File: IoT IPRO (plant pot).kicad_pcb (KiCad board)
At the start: 2 copper layers, 82 x 56 mm, 15 parts, among them Q1 Q_DUAL_NMOS_S1G1S2G2D1D1D2D2, U1 DS18S20, U3 AP9101C-SOT25

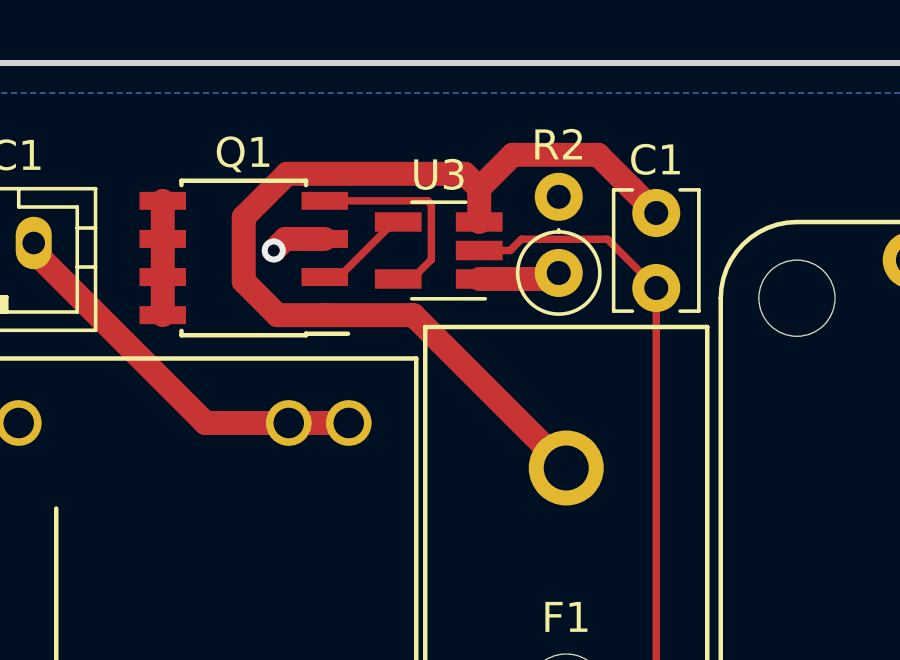
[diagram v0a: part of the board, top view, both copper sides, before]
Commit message: Switch AP9101C to SOT-26 :(
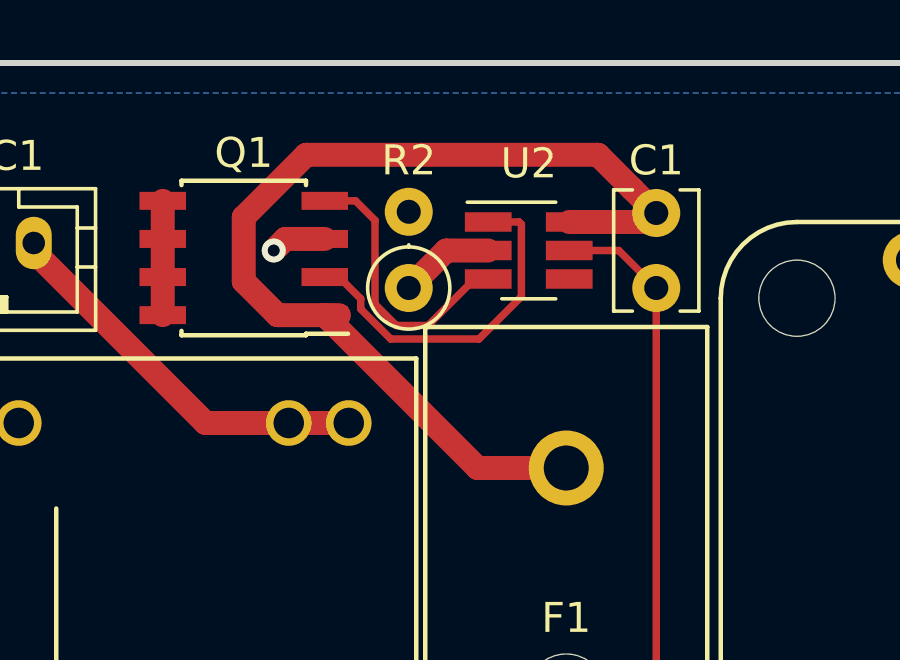
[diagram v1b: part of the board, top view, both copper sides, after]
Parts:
- removed U3: AP9101C-SOT25, Package_TO_SOT_SMD:SOT-23-5_HandSoldering
- added U2: AP9101C-SOT26, TO_SOT_Packages_SMD:SOT-23-6_Handsoldering, F.Cu at (81.5, 38.2)
- moved R2 5.02 mm to (77.5, 39.5)
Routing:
- net Net-(Q1-Pad2): track 3.21 -> 11.7 mm
- net Net-(C1-Pad1): track 30.4 -> 27.1 mm
- net Net-(Q1-Pad4): track 6.81 -> 9.45 mm
- net Net-(C1-Pad2): track 32.4 -> 34.4 mm

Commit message: Generate v1 Gerbers
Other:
- rule pad_to_mask_clearance: 0 -> 0.1
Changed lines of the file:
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@@
     (pad_size 1.5 1.5)
     (pad_drill 0.6)
-    (pad_to_mask_clearance 0)
+    (pad_to_mask_clearance 0.1)
     (solder_mask_min_width 0.25)
     (aux_axis_origin 0 0)
     (visible_elements 7FFFFFFF)
     (pcbplotparams
-      (layerselection 0x010fc_ffffffff)
+      (layerselection 0x010f0_ffffffff)
       (usegerberextensions false)
-      (usegerberattributes false)
+      (usegerberattributes true)
       (usegerberadvancedattributes false)
       (creategerberjobfile false)
@@
       (outputformat 1)
       (mirror false)
-      (drillshape 1)
+      (drillshape 0)
       (scaleselection 1)
-      (outputdirectory ""))
+      (outputdirectory "fab"))
   )
   (net 0 "")

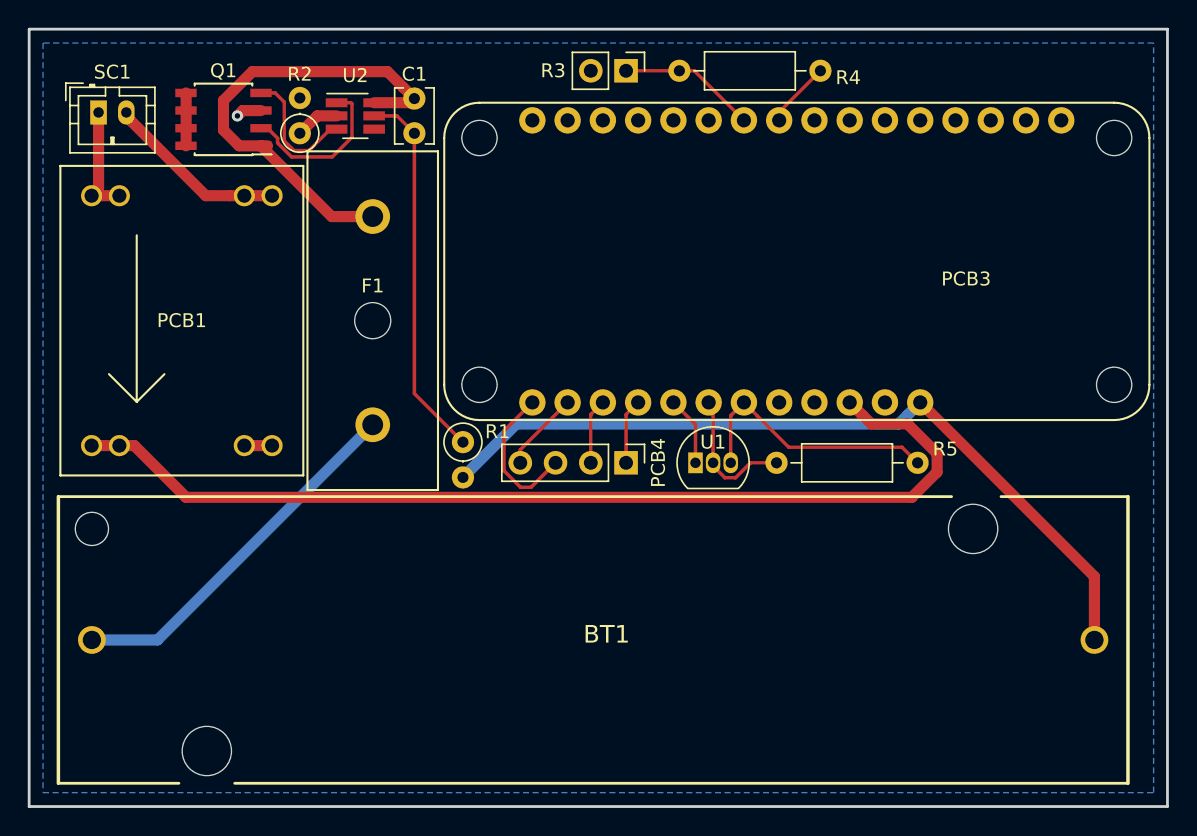
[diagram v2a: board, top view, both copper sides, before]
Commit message: Update PCB with new battery holder, U2 footprint
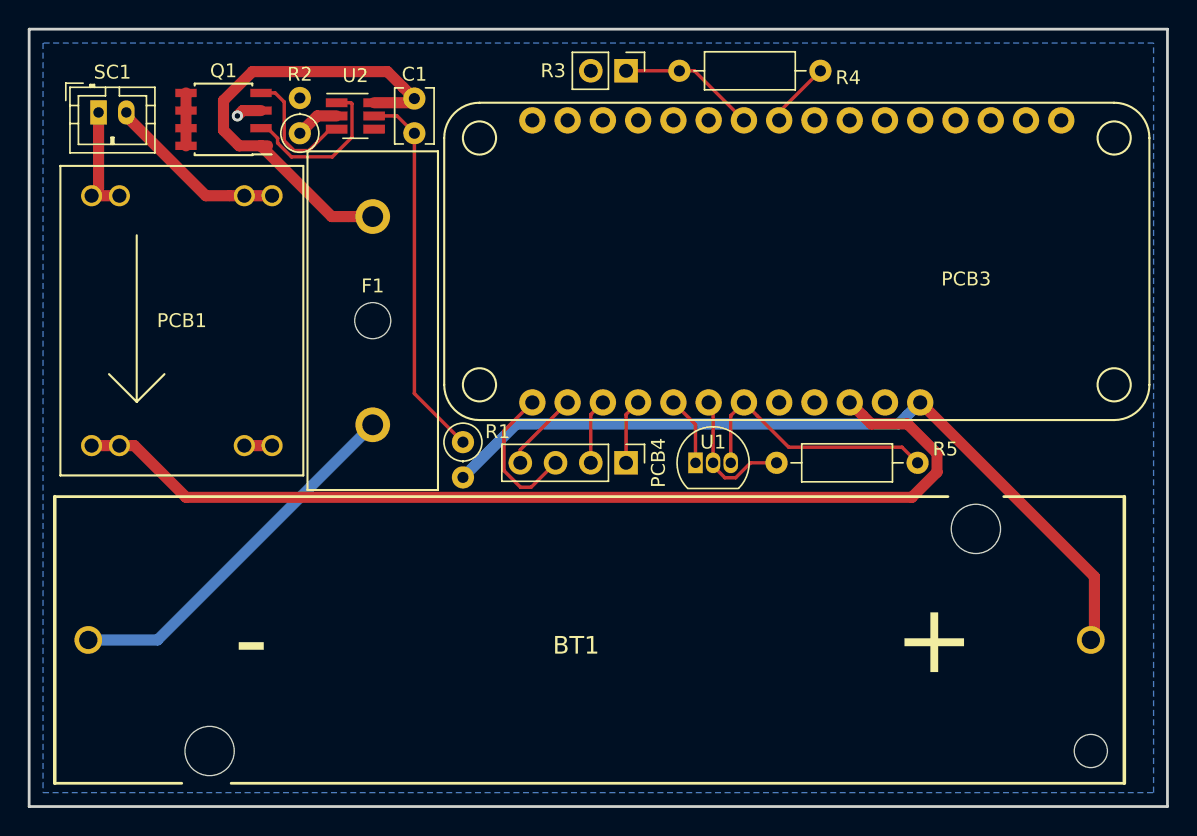
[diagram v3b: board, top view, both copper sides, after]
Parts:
- U2: footprint TO_SOT_Packages_SMD:SOT-23-6_Handsoldering -> Package_TO_SOT_SMD:SOT-23-6_Handsoldering
- moved BT1 57.3 mm to (71.0, 84.0), turned to 0 degrees
